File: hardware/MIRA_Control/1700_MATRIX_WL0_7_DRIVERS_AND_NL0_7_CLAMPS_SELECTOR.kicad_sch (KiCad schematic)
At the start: 50 parts, among them U1700 ADG5434, U1701 ADG5434, U1702 ADG5412, U1703 ADG5412, U1704 SN74LVC1G32, U1705 ADG5408

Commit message: Protect unpowered signal domains and qualify local supplies; retain startup and fault interlocks
MIRA-Startup-Patch: 7ffae17756ebcf923eff1212bb1aade8fbdfae03a9ca8ecebc69d3da3d3b4ba2
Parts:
- U1700, U1701: value ADG5434 -> TMUX7234PWR; symbol MIRA_RevA:ADG5434_MIRA_MAT -> MIRA_RevA:TMUX7234PWR_SIGNAL_MIRA; MPN ADG5434BRUZ -> TMUX7234PWR; Manufacturer Analog Devices -> Texas Instruments
- U1702, U1703: value ADG5412 -> TMUX7212PWR; symbol MIRA_RevA:ADG5412_MIRA_MAT -> MIRA_RevA:TMUX7212PWR_SIGNAL_MIRA; MPN ADG5412BRUZ -> TMUX7212PWR; Manufacturer Analog Devices -> Texas Instruments
- U1705: value ADG5408 -> TMUX7208PWR; symbol MIRA_RevA:ADG5408_MIRA_MAT -> MIRA_RevA:TMUX7208PWR_SIGNAL_MIRA; MPN ADG5408BRUZ -> TMUX7208PWR; Manufacturer Analog Devices -> Texas Instruments
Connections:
- net GND: now also U1700.15 (EN_N), U1701.15 (EN_N)
- no-connect marks 4 -> 2

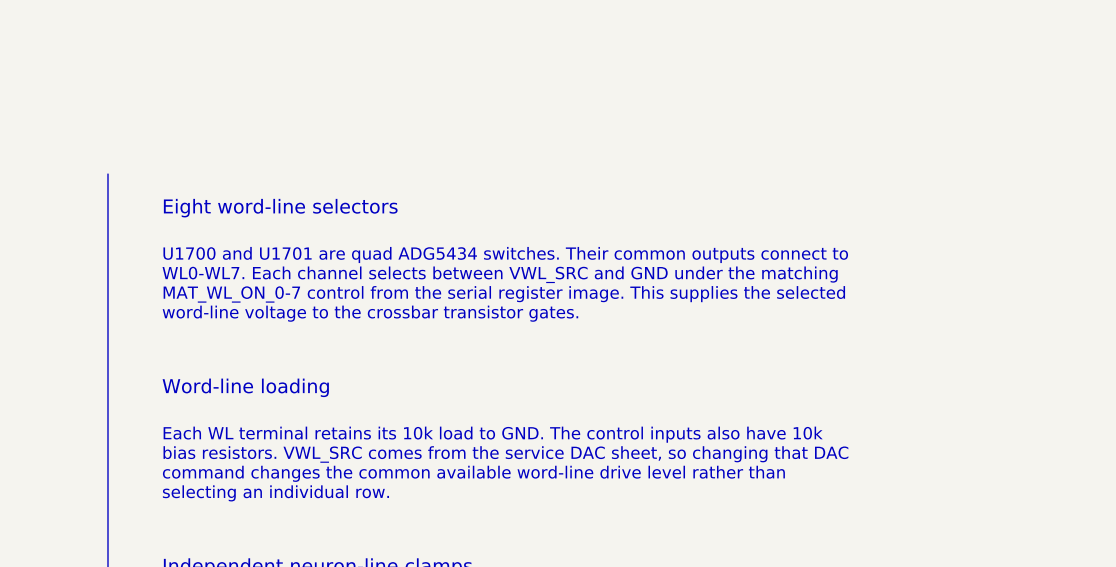
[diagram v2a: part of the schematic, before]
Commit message: MIRA.05: analog requirements and schematic fixes
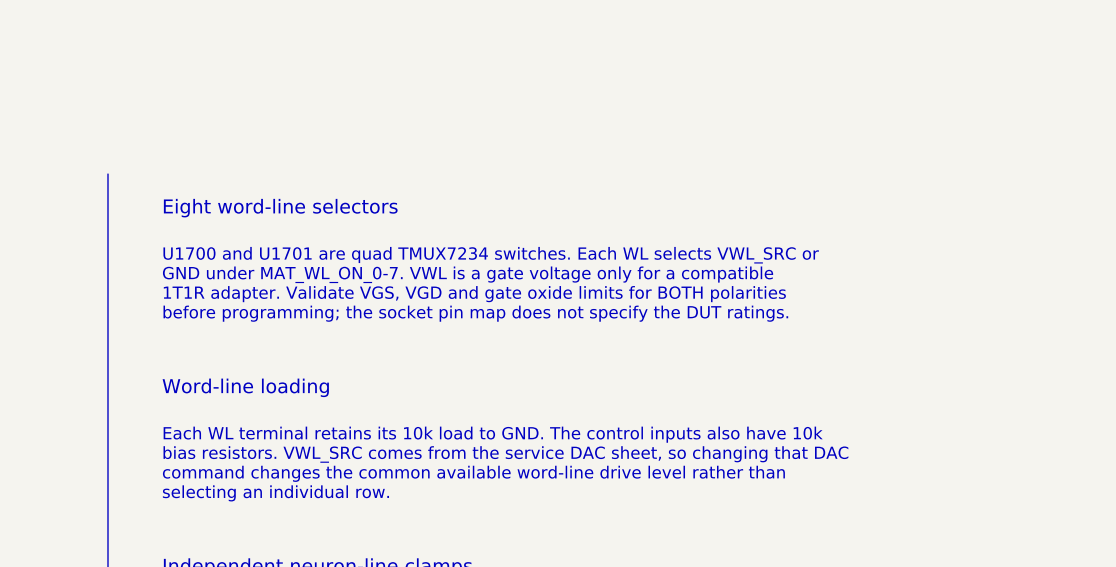
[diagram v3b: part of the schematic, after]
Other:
- note added: "U1700 and U1701 are quad TMUX7234 switches. Each WL selects VWL_SRC or GND under MAT_WL_ON_0-7. VWL is a gate voltage only for a compatible 1T1R adapter. Validate VGS, VGD and gate oxide limits for BOTH polarities before programming; the socket pin map does not specify the DUT ratings."
- note removed: "U1700 and U1701 are quad ADG5434 switches. Their common outputs connect to WL0-WL7. Each channel selects between VWL_SRC and GND under the matching MAT_WL_ON_0-7 control from the serial register image. This supplies the selected word-line voltage to the crossbar transistor gates."
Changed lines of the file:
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@@
 		)
 	)
-	(text "U1700 and U1701 are quad ADG5434 switches. Their common outputs connect to\nWL0-WL7. Each channel selects between VWL_SRC and GND under the matching\nMAT_WL_ON_0-7 control from the serial register image. This supplies the selected\nword-line voltage to the crossbar transistor gates."
-		(exclude_from_sim no)
-		(at 315 42.34 0)
-		(effects
-			(font
-				(size 1.35 1.35)
-				(color 0 70 160 1)
-			)
-			(justify left top)
-		)
-	)
+	(text "U1700 and U1701 are quad TMUX7234 switches. Each WL selects VWL_SRC or\nGND under MAT_WL_ON_0-7. VWL is a gate voltage only for a compatible\n1T1R adapter. Validate VGS, VGD and gate oxide limits for BOTH polarities\nbefore programming; the socket pin map does not specify the DUT ratings." (exclude_from_sim no) (at 315 42.34 0) (effects (font (size 1.35 1.35) (color 0 70 160 1)) (justify left top)))
 	(text "Word-line loading"
 		(exclude_from_sim no)

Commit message: Review MIRA.06 components, connectors and assembly
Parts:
- C1700, C1701, C1702, C1703, C1704, C1705, C1706, C1707, C1708, C1710: MPN (none) -> CC0603KRX7R9BB104; Manufacturer Murata -> YAGEO
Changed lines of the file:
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@@
 			)
 		)
-		(property "Datasheet" ""
+		(property "Datasheet" "https://yageogroup.com/component-documentation/download/specsheet/CC0603KRX7R9BB104"
 			(at 66.04 170.815 0)
 			(hide yes)
@@
 			)
 		)
-		(property "Description" "100n rail bypass, 35 V minimum"
+		(property "Description" "100n F nominal; 50 V, X7R, 10%; 0603; MIRA.06 assigned MPN; effective capacitance at bias/temperature requires qualification"
 			(at 66.04 170.815 0)
 			(hide yes)
@@
 			)
 		)
-		(property "MPN" ""
+		(property "MPN" "CC0603KRX7R9BB104"
 			(at 66.04 170.815 0)
 			(hide yes)
@@
 			)
 		)
-		(property "Manufacturer" "Murata"
+		(property "Manufacturer" "YAGEO"
 			(at 66.04 170.815 0)
 			(hide yes)
@@
 			)
 		)
-		(property "Datasheet" ""
+		(property "Datasheet" "https://yageogroup.com/component-documentation/download/specsheet/CC0603KRX7R9BB104"
 			(at 207.01 107.95 0)
 			(hide yes)
@@
 			)
 		)
-		(property "Description" "100n rail bypass, 35 V minimum"
+		(property "Description" "100n F nominal; 50 V, X7R, 10%; 0603; MIRA.06 assigned MPN; effective capacitance at bias/temperature requires qualification"
 			(at 207.01 107.95 0)
 			(hide yes)
@@
 			)
 		)
-		(property "MPN" ""
+		(property "MPN" "CC0603KRX7R9BB104"
 			(at 207.01 107.95 0)
 			(hide yes)
@@
 			)
 		)
-		(property "Manufacturer" "Murata"
+		(property "Manufacturer" "YAGEO"
 			(at 207.01 107.95 0)
 			(hide yes)
@@
 			)
 		)
-		(property "Datasheet" ""
+		(property "Datasheet" "https://yageogroup.com/component-documentation/download/specsheet/CC0603KRX7R9BB104"
 			(at 207.01 100.33 0)
 			(hide yes)
@@
 			)
 		)
-		(property "Description" "100n rail bypass, 35 V minimum"
+		(property "Description" "100n F nominal; 50 V, X7R, 10%; 0603; MIRA.06 assigned MPN; effective capacitance at bias/temperature requires qualification"
 			(at 207.01 100.33 0)
 			(hide yes)
@@
 			)
 		)
-		(property "MPN" ""
+		(property "MPN" "CC0603KRX7R9BB104"
 			(at 207.01 100.33 0)
 			(hide yes)
@@
 			)
 		)
-		(property "Manufacturer" "Murata"
+		(property "Manufacturer" "YAGEO"
 			(at 207.01 100.33 0)
 			(hide yes)
@@
 			)
 		)
-		(property "Datasheet" ""
+		(property "Datasheet" "https://yageogroup.com/component-documentation/download/specsheet/CC0603KRX7R9BB104"
 			(at 236.855 170.815 0)
 			(hide yes)
@@
 			)
 		)
-		(property "Description" "100n rail bypass, 35 V minimum"
+		(property "Description" "100n F nominal; 50 V, X7R, 10%; 0603; MIRA.06 assigned MPN; effective capacitance at bias/temperature requires qualification"
 			(at 236.855 170.815 0)
 			(hide yes)
@@
 			)
 		)
-		(property "MPN" ""
+		(property "MPN" "CC0603KRX7R9BB104"
 			(at 236.855 170.815 0)
 			(hide yes)
@@
 			)
 		)
-		(property "Manufacturer" "Murata"
+		(property "Manufacturer" "YAGEO"
 			(at 236.855 170.815 0)
 			(hide yes)
@@
 			)
 		)
-		(property "Datasheet" ""
+		(property "Datasheet" "https://yageogroup.com/component-documentation/download/specsheet/CC0603KRX7R9BB104"
 			(at 111.76 170.815 0)
 			(hide yes)
@@
 			)
 		)
-		(property "Description" "100n rail bypass, 35 V minimum"
+		(property "Description" "100n F nominal; 50 V, X7R, 10%; 0603; MIRA.06 assigned MPN; effective capacitance at bias/temperature requires qualification"
 			(at 111.76 170.815 0)
 			(hide yes)
@@
 			)
 		)
-		(property "MPN" ""
+		(property "MPN" "CC0603KRX7R9BB104"
 			(at 111.76 170.815 0)
 			(hide yes)
@@
 			)
 		)
-		(property "Manufacturer" "Murata"
+		(property "Manufacturer" "YAGEO"
 			(at 111.76 170.815 0)
 			(hide yes)
@@
 			)
 		)
-		(property "Datasheet" ""
+		(property "Datasheet" "https://yageogroup.com/component-documentation/download/specsheet/CC0603KRX7R9BB104"
 			(at 207.01 132.08 0)
 			(hide yes)
@@
 			)
 		)
-		(property "Description" "100n rail bypass, 35 V minimum"
+		(property "Description" "100n F nominal; 50 V, X7R, 10%; 0603; MIRA.06 assigned MPN; effective capacitance at bias/temperature requires qualification"
 			(at 207.01 132.08 0)
 			(hide yes)
@@
 			)
 		)
-		(property "MPN" ""
+		(property "MPN" "CC0603KRX7R9BB104"
 			(at 207.01 132.08 0)
 			(hide yes)
@@
 			)
 		)
-		(property "Manufacturer" "Murata"
+		(property "Manufacturer" "YAGEO"
 			(at 207.01 132.08 0)
 			(hide yes)
@@
 			)
 		)
-		(property "Datasheet" ""
+		(property "Datasheet" "https://yageogroup.com/component-documentation/download/specsheet/CC0603KRX7R9BB104"
 			(at 275.59 133.35 0)
 			(hide yes)
@@
 			)
 		)
-		(property "Description" "100n rail bypass, 35 V minimum"
+		(property "Description" "100n F nominal; 50 V, X7R, 10%; 0603; MIRA.06 assigned MPN; effective capacitance at bias/temperature requires qualification"
 			(at 275.59 133.35 0)
 			(hide yes)
@@
 			)
 		)
-		(property "MPN" ""
+		(property "MPN" "CC0603KRX7R9BB104"
 			(at 275.59 133.35 0)
 			(hide yes)
@@
 			)
 		)
-		(property "Manufacturer" "Murata"
+		(property "Manufacturer" "YAGEO"
 			(at 275.59 133.35 0)
 			(hide yes)
@@
 			)
 		)
-		(property "Datasheet" ""
+		(property "Datasheet" "https://yageogroup.com/component-documentation/download/specsheet/CC0603KRX7R9BB104"
 			(at 191.135 170.815 0)
 			(hide yes)
@@
 			)
 		)
-		(property "Description" "100n rail bypass, 35 V minimum"
+		(property "Description" "100n F nominal; 50 V, X7R, 10%; 0603; MIRA.06 assigned MPN; effective capacitance at bias/temperature requires qualification"
 			(at 191.135 170.815 0)
 			(hide yes)
@@
 			)
 		)
-		(property "MPN" ""
+		(property "MPN" "CC0603KRX7R9BB104"
 			(at 191.135 170.815 0)
 			(hide yes)
@@
 			)
 		)
-		(property "Manufacturer" "Murata"
+		(property "Manufacturer" "YAGEO"
 			(at 191.135 170.815 0)
 			(hide yes)
@@
 			)
 		)
-		(property "Datasheet" ""
+		(property "Datasheet" "https://yageogroup.com/component-documentation/download/specsheet/CC0603KRX7R9BB104"
 			(at 207.01 139.7 0)
 			(hide yes)
@@
 			)
 		)
-		(property "Description" "100n rail bypass, 35 V minimum"
+		(property "Description" "100n F nominal; 50 V, X7R, 10%; 0603; MIRA.06 assigned MPN; effective capacitance at bias/temperature requires qualification"
 			(at 207.01 139.7 0)
 			(hide yes)
@@
 			)
 		)
-		(property "MPN" ""
+		(property "MPN" "CC0603KRX7R9BB104"
 			(at 207.01 139.7 0)
 			(hide yes)
@@
 			)
 		)
-		(property "Manufacturer" "Murata"
+		(property "Manufacturer" "YAGEO"
 			(at 207.01 139.7 0)
 			(hide yes)
@@
 			)
 		)
-		(property "Datasheet" ""
+		(property "Datasheet" "https://yageogroup.com/component-documentation/download/specsheet/CC0603KRX7R9BB104"
 			(at 251.46 133.35 0)
 			(hide yes)
@@
 			)
 		)
-		(property "Description" "100n rail bypass, 35 V minimum"
+		(property "Description" "100n F nominal; 50 V, X7R, 10%; 0603; MIRA.06 assigned MPN; effective capacitance at bias/temperature requires qualification"
 			(at 251.46 133.35 0)
 			(hide yes)
@@
 			)
 		)
-		(property "MPN" ""
+		(property "MPN" "CC0603KRX7R9BB104"
 			(at 251.46 133.35 0)
 			(hide yes)
@@
 			)
 		)
-		(property "Manufacturer" "Murata"
+		(property "Manufacturer" "YAGEO"
 			(at 251.46 133.35 0)
 			(hide yes)
